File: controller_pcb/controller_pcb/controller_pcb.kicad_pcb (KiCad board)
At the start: 2 copper layers, 31 parts, among them J1 USB_B_Micro, J2 Conn_01x04_Male

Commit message: started wiring schematic
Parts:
- removed J2: Conn_01x04_Male, Connector_PinHeader_2.54mm:PinHeader_1x04_P2.54mm_Vertical
- added C10: 30p, Capacitor_SMD:C_0805_2012Metric, F.Cu at (127.0, 104.1)
- added C11: 30p, Capacitor_SMD:C_0805_2012Metric, F.Cu at (126.0, 95.0)
- added FLASH1: JTAG/SWD, Connector_PinHeader_2.54mm:PinHeader_2x10_P2.54mm_Vertical, F.Cu at (135.9, 64.8)
- added Y1: 8MHz, Crystal:Crystal_SMD_5032-2Pin_5.0x3.2mm, F.Cu at (119.4, 99.1)
- FB1: footprint Inductor_SMD:L_0603_1608Metric -> Resistor_SMD:R_0805_2012Metric
- moved S12 180.4 mm to (269.2, 68.6)
- moved S5 156.7 mm to (233.7, 92.4)
- moved S8 154.5 mm to (247.0, 105.1)
- moved S3 149.6 mm to (221.6, 105.1)
- moved S11 142.5 mm to (234.3, 120.4)
- moved S7 140.8 mm to (238.8, 35.6)
- moved JS2 75.4 mm to (101.6, 144.8)
- moved S10 73.6 mm to (48.3, 119.4)
- moved C1 65.7 mm to (155.9, 53.3)
- moved FB1 60.4 mm to (144.8, 45.7)
- moved D1 58.1 mm to (159.2, 33.0)
- moved S9 49.7 mm to (35.6, 106.7)
- moved S4 46.8 mm to (48.9, 36.6)
- moved S1 46.4 mm to (61.0, 106.7)
- moved S2 46.3 mm to (48.3, 94.0)
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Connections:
- MCU1 pad 12: unconnected-(MCU1-Pad12) -> Net-(MCU1-Pad12)
- MCU1 pad 13: unconnected-(MCU1-Pad13) -> Net-(MCU1-Pad13)
- MCU1 pad 7: Net-(J2-Pad2) -> unconnected-(MCU1-Pad7)
- MCU1 pad 72: unconnected-(MCU1-Pad72) -> /SW_DIO
- MCU1 pad 76: unconnected-(MCU1-Pad76) -> /SW_CLK
- MCU1 pad 8: Net-(J2-Pad3) -> unconnected-(MCU1-Pad8)
- MCU1 pad 94: unconnected-(MCU1-Pad94) -> GND

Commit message: finalized pcb layout, no edges have been made
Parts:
- moved C8 80.4 mm to (90.3, 108.3), turned to 180 degrees
- moved C9 77.4 mm to (90.3, 95.6), turned to 180 degrees
- moved L1 66.1 mm to (99.1, 101.6), turned to 180 degrees
- moved C10 45.5 mm to (92.7, 74.3)
- moved Y1 36.4 mm to (104.1, 66.0)
- moved C5 28.4 mm to (172.5, 120.4), turned to -90 degrees
- moved S12 27.9 mm to (241.3, 68.6)
- moved C4 24.1 mm to (166.1, 120.4), turned to -90 degrees
- moved MCU1 24.0 mm to (158.6, 105.1)
- moved FLASH1 24.0 mm to (147.2, 86.0)
- moved C11 23.8 mm to (114.3, 74.3)
- moved C3 21.8 mm to (159.3, 120.4), turned to -90 degrees
- moved CONV1 19.2 mm to (165.2, 62.0)
- moved C1 18.6 mm to (164.9, 69.6)
- moved D1 18.6 mm to (168.2, 49.3)
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
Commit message: small change
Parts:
- moved JS2 1.91 mm to (85.7, 144.8)
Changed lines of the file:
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@@
   )
   (footprint "COM-09032:XDCR_COM-09032" (layer "F.Cu")
-    (at 83.82 144.78)
+    (at 85.725 144.78)
     (property "MANUFACTURER" "SparkFun Electronics")
     (property "MAXIMUM_PACKAGE_HEIGHT" "30.1mm")

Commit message: finialized pcb arrangment
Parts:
- moved JS2 29.2 mm to (114.9, 145.4)
- moved S1 29.2 mm to (88.9, 112.4)
- moved S9 29.2 mm to (66.0, 112.4)
- moved S10 29.2 mm to (77.5, 123.8)
- moved S2 29.2 mm to (77.5, 101.0)
- moved S4 29.2 mm to (72.4, 54.7)
- moved S6 29.2 mm to (72.4, 69.2)
- moved C10 25.7 mm to (118.1, 70.5)
- moved C8 25.7 mm to (115.7, 104.5)
- moved C9 25.7 mm to (115.7, 91.8)
- moved Y1 25.7 mm to (129.5, 62.2)
- moved C11 25.7 mm to (139.7, 70.5)
- moved L1 25.7 mm to (124.5, 97.8)
- moved JS1 16.7 mm to (181.4, 145.4)
- moved S11 16.7 mm to (218.9, 123.8)
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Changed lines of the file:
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@@
   (net 128 "unconnected-(MCU1-Pad8)")
   (footprint "Connector_PinHeader_2.54mm:PinHeader_2x10_P2.54mm_Vertical" (layer "F.Cu")
-    (at 147.221 85.984 90)
+    (at 151.77 86.365 90)
     (descr "Through hole straight pin header, 2x10, 2.54mm pitch, double rows")
     (tags "Through hole pin header THT 2x10 2.54mm double row")
@@
   )
   (footprint "COM-09032:XDCR_COM-09032" (layer "F.Cu")
-    (at 85.725 144.78)
+    (at 114.935 145.415)
     (property "MANUFACTURER" "SparkFun Electronics")
     (property "MAXIMUM_PACKAGE_HEIGHT" "30.1mm")
@@
   )
   (footprint "Capacitor_SMD:C_0805_2012Metric" (layer "F.Cu")
-    (at 164.869 69.596)
+    (at 169.418 69.977)
     (descr "Capacitor SMD 0805 (2012 Metric), square (rectangular) end terminal, IPC_7351 nominal, (Body size source: IPC-SM-782 page 76, https://www.pcb-3d.com/wordpress/wp-content/uploads/ipc-sm-782a_amendment_1_and_2.pdf, https://docs.google.com/spreadsheets/d/1BsfQQcO9C6DZCsRaXUlFlo91Tg2WpOkGARC1WS5S8t0/edit?usp=sharing), generated with kicad-footprint-generator")
     (tags "capacitor")
@@
   )
   (footprint "Inductor_SMD:L_0402_1005Metric" (layer "F.Cu")
-    (at 99.06 101.6 180)
+    (at 124.46 97.79 180)
     (descr "Inductor SMD 0402 (1005 Metric), square (rectangular) end terminal, IPC_7351 nominal, (Body size source: http://www.tortai-tech.com/upload/download/2011102023233369053.pdf), generated with kicad-footprint-generator")
     (tags "inductor")
@@
   )
   (footprint "B3F-1000:SW_B3F-1000" (layer "F.Cu")
-    (at 43.18 54.05)
+    (at 72.39 54.685)
     (property "MANUFACTURER" "Omron")
     (property "Sheetfile" "controller_pcb.kicad_sch")
@@
   )
   (footprint "Crystal:Crystal_SMD_5032-2Pin_5.0x3.2mm" (layer "F.Cu")
-    (at 104.14 66.04)
+    (at 129.54 62.23)
     (descr "SMD Crystal SERIES SMD2520/2 http://www.icbase.com/File/PDF/HKC/HKC00061008.pdf, 5.0x3.2mm^2 package")
     (tags "SMD SMT crystal")
@@
   )
   (footprint "B3F-1000:SW_B3F-1000" (layer "F.Cu")
-    (at 241.3 68.58)
+    (at 224.59 69.152846)
     (property "MANUFACTURER" "Omron")
     (property "Sheetfile" "controller_pcb.kicad_sch")
@@
   )
   (footprint "B3F-1000:SW_B3F-1000" (layer "F.Cu")
-    (at 48.26 100.33)
+    (at 77.47 100.965)
     (property "MANUFACTURER" "Omron")
     (property "Sheetfile" "controller_pcb.kicad_sch")
@@
   )
   (footprint "B3F-1000:SW_B3F-1000" (layer "F.Cu")
-    (at 36.83 111.76)
+    (at 66.04 112.395)
     (property "MANUFACTURER" "Omron")
     (property "Sheetfile" "controller_pcb.kicad_sch")
@@
   )
   (footprint "Capacitor_SMD:C_0805_2012Metric" (layer "F.Cu")
-    (at 90.274 95.631 180)
+    (at 115.674 91.821 180)
     (descr "Capacitor SMD 0805 (2012 Metric), square (rectangular) end terminal, IPC_7351 nominal, (Body size source: IPC-SM-782 page 76, https://www.pcb-3d.com/wordpress/wp-content/uploads/ipc-sm-782a_amendment_1_and_2.pdf, https://docs.google.com/spreadsheets/d/1BsfQQcO9C6DZCsRaXUlFlo91Tg2WpOkGARC1WS5S8t0/edit?usp=sharing), generated with kicad-footprint-generator")
     (tags "capacitor")
@@
   )
   (footprint "B3F-1000:SW_B3F-1000" (layer "F.Cu")
-    (at 59.69 111.76)
+    (at 88.9 112.395)
     (property "MANUFACTURER" "Omron")
     (property "Sheetfile" "controller_pcb.kicad_sch")
@@
   )
   (footprint "B3F-1000:SW_B3F-1000" (layer "F.Cu")
-    (at 235.585 100.33)
+    (at 218.875 100.902846)
     (property "MANUFACTURER" "Omron")
     (property "Sheetfile" "controller_pcb.kicad_sch")
@@
   )
   (footprint "Capacitor_SMD:C_0805_2012Metric" (layer "F.Cu")
-    (at 90.274 108.331 180)
+    (at 115.674 104.521 180)
     (descr "Capacitor SMD 0805 (2012 Metric), square (rectangular) end terminal, IPC_7351 nominal, (Body size source: IPC-SM-782 page 76, https://www.pcb-3d.com/wordpress/wp-content/uploads/ipc-sm-782a_amendment_1_and_2.pdf, https://docs.google.com/spreadsheets/d/1BsfQQcO9C6DZCsRaXUlFlo91Tg2WpOkGARC1WS5S8t0/edit?usp=sharing), generated with kicad-footprint-generator")
     (tags "capacitor")
@@
   )
   (footprint "B3F-1000:SW_B3F-1000" (layer "F.Cu")
-    (at 48.26 123.19)
+    (at 77.47 123.825)
     (property "MANUFACTURER" "Omron")
     (property "Sheetfile" "controller_pcb.kicad_sch")
@@
   )
   (footprint "Capacitor_SMD:C_0805_2012Metric" (layer "F.Cu")
-    (at 92.71 74.295)
+    (at 118.11 70.485)
     (descr "Capacitor SMD 0805 (2012 Metric), square (rectangular) end terminal, IPC_7351 nominal, (Body size source: IPC-SM-782 page 76, https://www.pcb-3d.com/wordpress/wp-content/uploads/ipc-sm-782a_amendment_1_and_2.pdf, https://docs.google.com/spreadsheets/d/1BsfQQcO9C6DZCsRaXUlFlo91Tg2WpOkGARC1WS5S8t0/edit?usp=sharing), generated with kicad-footprint-generator")
     (tags "capacitor")
@@
   )
   (footprint "Capacitor_SMD:C_0805_2012Metric" (layer "F.Cu")
-    (at 114.3 74.295)
+    (at 139.7 70.485)
     (descr "Capacitor SMD 0805 (2012 Metric), square (rectangular) end terminal, IPC_7351 nominal, (Body size source: IPC-SM-782 page 76, https://www.pcb-3d.com/wordpress/wp-content/uploads/ipc-sm-782a_amendment_1_and_2.pdf, https://docs.google.com/spreadsheets/d/1BsfQQcO9C6DZCsRaXUlFlo91Tg2WpOkGARC1WS5S8t0/edit?usp=sharing), generated with kicad-footprint-generator")
     (tags "capacitor")
@@
   )
   (footprint "B3F-1000:SW_B3F-1000" (layer "F.Cu")
-    (at 43.18 68.58)
+    (at 72.39 69.215)
     (property "MANUFACTURER" "Omron")
     (property "Sheetfile" "controller_pcb.kicad_sch")
@@
   )
   (footprint "Resistor_SMD:R_0805_2012Metric" (layer "F.Cu")
-    (at 153.759 61.976)
+    (at 158.308 62.357)
     (descr "Resistor SMD 0805 (2012 Metric), square (rectangular) end terminal, IPC_7351 nominal, (Body size source: IPC-SM-782 page 72, https://www.pcb-3d.com/wordpress/wp-content/uploads/ipc-sm-782a_amendment_1_and_2.pdf), generated with kicad-footprint-generator")
     (tags "resistor")
@@
   )
   (footprint "Package_TO_SOT_SMD:SOT-23" (layer "F.Cu")
-    (at 165.189 61.976)
+    (at 169.738 62.357)
     (descr "SOT, 3 Pin (https://www.jedec.org/system/files/docs/to-236h.pdf variant AB), generated with kicad-footprint-generator ipc_gullwing_generator.py")
     (tags "SOT TO_SOT_SMD")
@@
   )
   (footprint "B3F-1000:SW_B3F-1000" (layer "F.Cu")
-    (at 241.3 52.705)
+    (at 224.59 53.277846)
     (property "MANUFACTURER" "Omron")
     (property "Sheetfile" "controller_pcb.kicad_sch")
@@
   )
   (footprint "B3F-1000:SW_B3F-1000" (layer "F.Cu")
-    (at 224.155 111.76)
+    (at 207.445 112.332846)
     (property "MANUFACTURER" "Omron")
     (property "Sheetfile" "controller_pcb.kicad_sch")
@@
   )
   (footprint "B3F-1000:SW_B3F-1000" (layer "F.Cu")
-    (at 235.585 123.19)
+    (at 218.875 123.762846)
     (property "MANUFACTURER" "Omron")
     (property "Sheetfile" "controller_pcb.kicad_sch")
@@
   )
   (footprint "COM-09032:XDCR_COM-09032" (layer "F.Cu")
-    (at 198.12 144.78)
+    (at 181.41 145.352846)
     (property "MANUFACTURER" "SparkFun Electronics")
     (property "MAXIMUM_PACKAGE_HEIGHT" "30.1mm")
@@
   )
   (footprint "B3F-1000:SW_B3F-1000" (layer "F.Cu")
-    (at 247.015 111.76)
+    (at 230.305 112.332846)
     (property "MANUFACTURER" "Omron")
     (property "Sheetfile" "controller_pcb.kicad_sch")
@@
   )
   (footprint "Capacitor_SMD:C_0805_2012Metric" (layer "F.Cu")
-    (at 153.759 69.596)
+    (at 158.308 69.977)
     (descr "Capacitor SMD 0805 (2012 Metric), square (rectangular) end terminal, IPC_7351 nominal, (Body size source: IPC-SM-782 page 76, https://www.pcb-3d.com/wordpress/wp-content/uploads/ipc-sm-782a_amendment_1_and_2.pdf, https://docs.google.com/spreadsheets/d/1BsfQQcO9C6DZCsRaXUlFlo91Tg2WpOkGARC1WS5S8t0/edit?usp=sharing), generated with kicad-footprint-generator")
     (tags "capacitor")

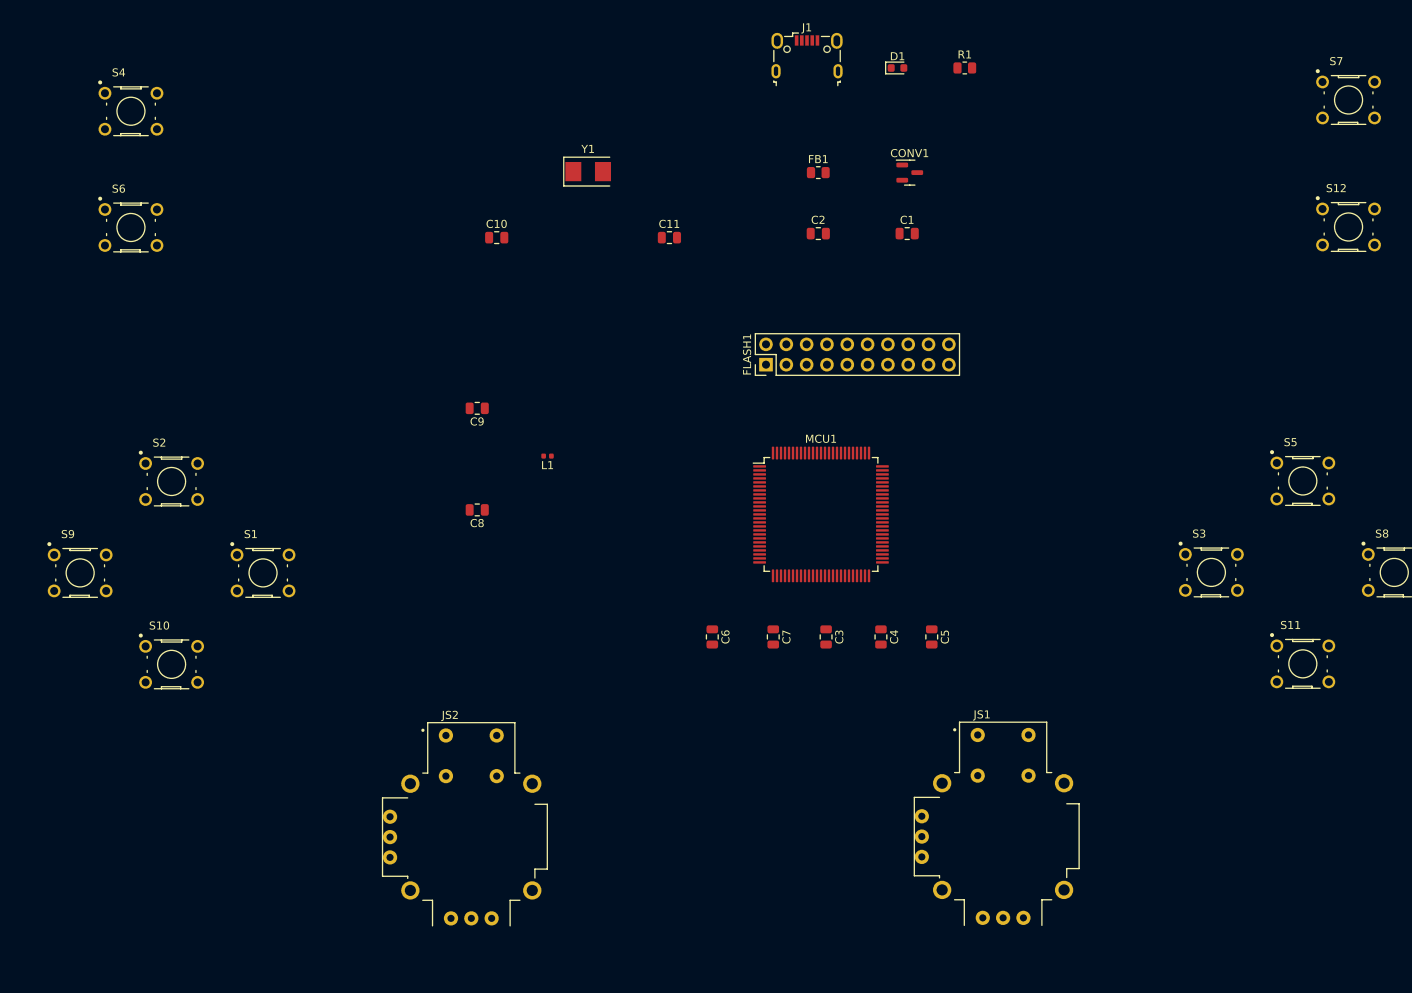
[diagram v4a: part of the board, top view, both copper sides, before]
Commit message: Added vias for GND pins
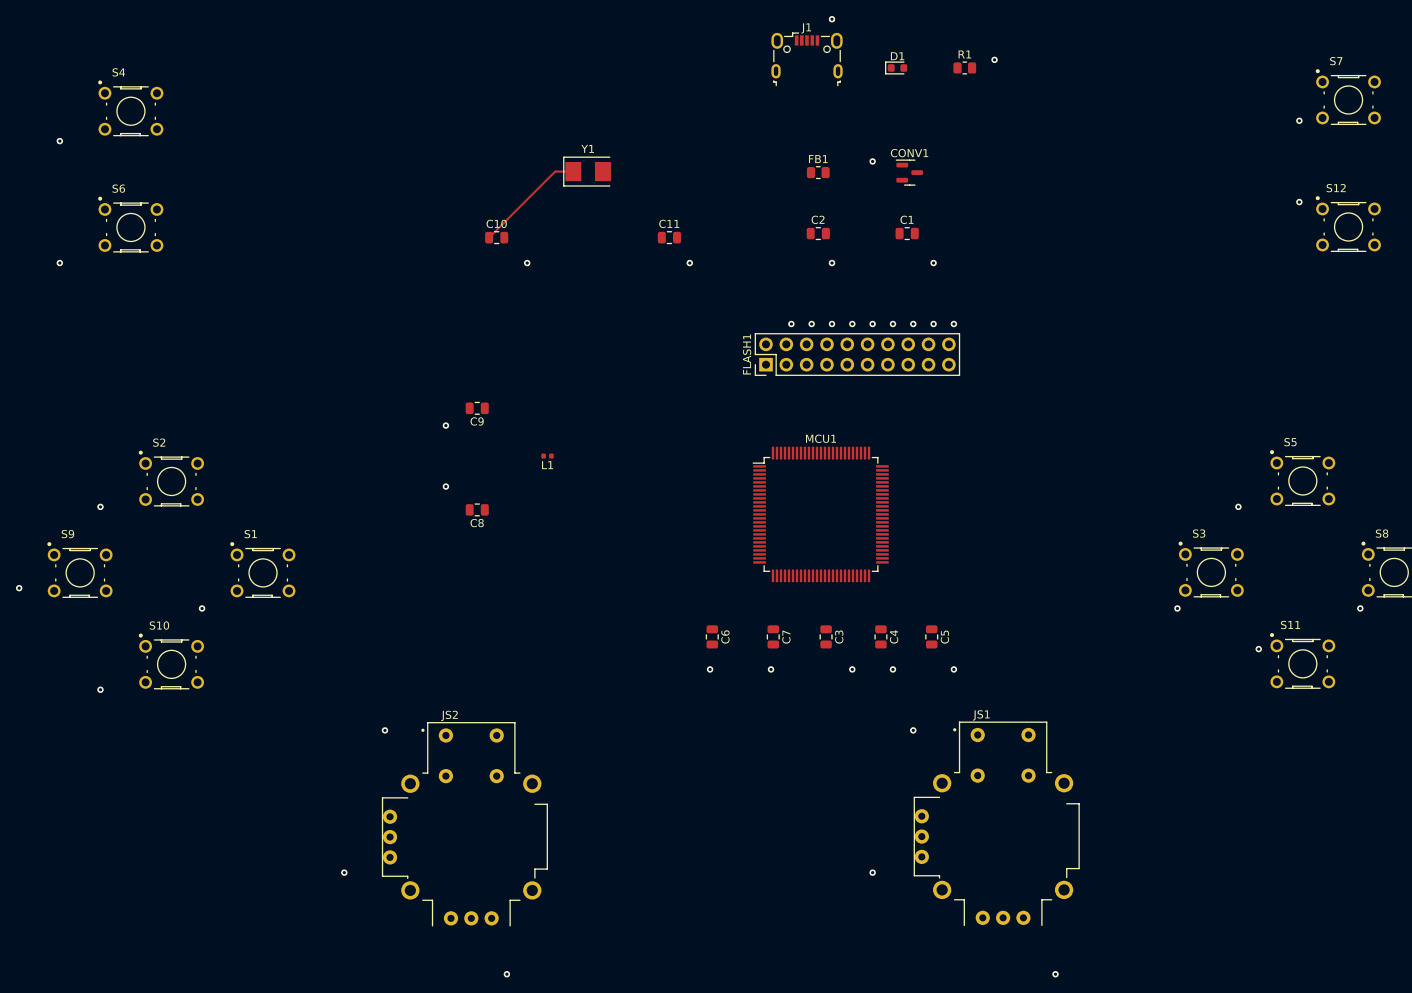
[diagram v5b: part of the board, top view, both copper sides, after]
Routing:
- net Net-(MCU1-Pad12): track 0.00 -> 13.9 mm
- net (no net): vias 0 -> 41
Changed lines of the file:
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@@
     )
   )
+  (via (at 165.1 60.96) (size 0.8) (drill 0.4) (layers "F.Cu" "B.Cu") (free) (net 0))
+  (via (at 167.64 81.28) (size 0.8) (drill 0.4) (layers "F.Cu" "B.Cu") (free) (net 0))
+  (via (at 121.92 73.66) (size 0.8) (drill 0.4) (layers "F.Cu" "B.Cu") (free) (net 0))
+  (via (at 160.02 81.28) (size 0.8) (drill 0.4) (layers "F.Cu" "B.Cu") (free) (net 0))
+  (via (at 58.42 114.3) (size 0.8) (drill 0.4) (layers "F.Cu" "B.Cu") (free) (net 0))
+  (via (at 111.76 101.6) (size 0.8) (drill 0.4) (layers "F.Cu" "B.Cu") (free) (net 0))
+  (via (at 203.2 116.84) (size 0.8) (drill 0.4) (layers "F.Cu" "B.Cu") (free) (net 0))
+  (via (at 160.02 73.66) (size 0.8) (drill 0.4) (layers "F.Cu" "B.Cu") (free) (net 0))
+  (via (at 180.34 48.26) (size 0.8) (drill 0.4) (layers "F.Cu" "B.Cu") (free) (net 0))
+  (via (at 165.1 149.86) (size 0.8) (drill 0.4) (layers "F.Cu" "B.Cu") (free) (net 0))
+  (via (at 157.48 81.28) (size 0.8) (drill 0.4) (layers "F.Cu" "B.Cu") (free) (net 0))
+  (via (at 187.96 162.56) (size 0.8) (drill 0.4) (layers "F.Cu" "B.Cu") (free) (net 0))
+  (via (at 175.26 124.46) (size 0.8) (drill 0.4) (layers "F.Cu" "B.Cu") (free) (net 0))
+  (via (at 144.78 124.46) (size 0.8) (drill 0.4) (layers "F.Cu" "B.Cu") (free) (net 0))
+  (via (at 172.72 73.66) (size 0.8) (drill 0.4) (layers "F.Cu" "B.Cu") (free) (net 0))
+  (via (at 63.5 73.66) (size 0.8) (drill 0.4) (layers "F.Cu" "B.Cu") (free) (net 0))
+  (via (at 162.56 124.46) (size 0.8) (drill 0.4) (layers "F.Cu" "B.Cu") (free) (net 0))
+  (via (at 218.44 66.04) (size 0.8) (drill 0.4) (layers "F.Cu" "B.Cu") (free) (net 0))
+  (via (at 104.14 132.08) (size 0.8) (drill 0.4) (layers "F.Cu" "B.Cu") (free) (net 0))
+  (via (at 175.26 81.28) (size 0.8) (drill 0.4) (layers "F.Cu" "B.Cu") (free) (net 0))
+  (via (at 68.58 104.14) (size 0.8) (drill 0.4) (layers "F.Cu" "B.Cu") (free) (net 0))
+  (via (at 142.24 73.66) (size 0.8) (drill 0.4) (layers "F.Cu" "B.Cu") (free) (net 0))
+  (via (at 99.06 149.86) (size 0.8) (drill 0.4) (layers "F.Cu" "B.Cu") (free) (net 0))
+  (via (at 111.76 93.98) (size 0.8) (drill 0.4) (layers "F.Cu" "B.Cu") (free) (net 0))
+  (via (at 210.82 104.14) (size 0.8) (drill 0.4) (layers "F.Cu" "B.Cu") (free) (net 0))
+  (via (at 81.28 116.84) (size 0.8) (drill 0.4) (layers "F.Cu" "B.Cu") (free) (net 0))
+  (via (at 167.64 124.46) (size 0.8) (drill 0.4) (layers "F.Cu" "B.Cu") (free) (net 0))
+  (via (at 160.02 43.18) (size 0.8) (drill 0.4) (layers "F.Cu" "B.Cu") (free) (net 0))
+  (via (at 154.94 81.28) (size 0.8) (drill 0.4) (layers "F.Cu" "B.Cu") (free) (net 0))
+  (via (at 162.56 81.28) (size 0.8) (drill 0.4) (layers "F.Cu" "B.Cu") (free) (net 0))
+  (via (at 218.44 55.88) (size 0.8) (drill 0.4) (layers "F.Cu" "B.Cu") (free) (net 0))
+  (via (at 170.18 132.08) (size 0.8) (drill 0.4) (layers "F.Cu" "B.Cu") (free) (net 0))
+  (via (at 152.4 124.46) (size 0.8) (drill 0.4) (layers "F.Cu" "B.Cu") (free) (net 0))
+  (via (at 213.36 121.92) (size 0.8) (drill 0.4) (layers "F.Cu" "B.Cu") (free) (net 0))
+  (via (at 119.38 162.56) (size 0.8) (drill 0.4) (layers "F.Cu" "B.Cu") (free) (net 0))
+  (via (at 226.06 116.84) (size 0.8) (drill 0.4) (layers "F.Cu" "B.Cu") (free) (net 0))
+  (via (at 172.72 81.28) (size 0.8) (drill 0.4) (layers "F.Cu" "B.Cu") (free) (net 0))
+  (via (at 165.1 81.28) (size 0.8) (drill 0.4) (layers "F.Cu" "B.Cu") (free) (net 0))
+  (via (at 63.5 58.42) (size 0.8) (drill 0.4) (layers "F.Cu" "B.Cu") (free) (net 0))
+  (via (at 68.58 127) (size 0.8) (drill 0.4) (layers "F.Cu" "B.Cu") (free) (net 0))
+  (via (at 170.18 81.28) (size 0.8) (drill 0.4) (layers "F.Cu" "B.Cu") (free) (net 0))
+  (segment (start 125.415 62.23) (end 117.16 70.485) (width 0.25) (layer "F.Cu") (net 11))
+  (segment (start 127.69 62.23) (end 125.415 62.23) (width 0.25) (layer "F.Cu") (net 11))
 )
